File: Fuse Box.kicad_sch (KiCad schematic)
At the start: 12 parts

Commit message: HUGE TOP LEVEL
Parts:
- F?: value (none) -> Fuse 3
- F?: value (none) -> Fuse 1
- F?: value (none) -> Fuse 4
- F?: value (none) -> Fuse 2
- K? (x4): value (none) -> Relay
- U?: value (none) -> DT_12_Pin
- U? (x2): value (none) -> Bridge
- U?: value (none) -> DTM04-12pb
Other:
- note added: "CANH and CANL Not Used on Fusebox, Was 4 PDM"
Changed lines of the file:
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@@
     (stroke (width 0) (type default) (color 0 0 0 0))
   )
+  (text "CANH and CANL Not Used on Fusebox, Was 4 PDM" (at 113.792 53.848 0)
+    (effects (font (size 1.27 1.27)) (justify left bottom))
+  )
   (global_label "Fan Power" (shape input) (at 75.184 29.972 180) (fields_autoplaced)
     (effects (font (size 1.27 1.27)) (justify right))
@@
     )
   )
-  (global_label "EFI Signal" (shape input) (at 149.098 33.782 0) (fields_autoplaced)
-    (effects (font (size 1.27 1.27)) (justify left))
-    (property "Intersheet References" "${INTERSHEET_REFS}" (id 0) (at 161.2478 33.7026 0)
+  (global_label "EFI Relay Signal" (shape input) (at 149.098 33.782 0) (fields_autoplaced)
+    (effects (font (size 1.27 1.27)) (justify left))
+    (property "Intersheet References" "${INTERSHEET_REFS}" (id 0) (at 167.3559 33.7026 0)
       (effects (font (size 1.27 1.27)) (justify left) hide)
     )
@@
     (in_bom yes) (on_board yes) (fields_autoplaced)
     (property "Reference" "K?" (id 0) (at 139.8905 60.452 0))
-    (property "Value" "" (id 1) (at 139.8905 62.992 0))
+    (property "Value" "Relay" (id 1) (at 139.8905 62.992 0))
     (property "Footprint" "" (id 2) (at 173.609 76.962 0)
       (effects (font (size 1.27 1.27)) hide)
@@
     (in_bom yes) (on_board yes) (fields_autoplaced)
     (property "Reference" "F?" (id 0) (at 82.296 134.112 90))
-    (property "Value" "" (id 1) (at 82.296 136.652 90))
+    (property "Value" "Fuse 3" (id 1) (at 82.296 136.652 90))
     (property "Footprint" "" (id 2) (at 82.296 138.684 90)
       (effects (font (size 1.27 1.27)) hide)
@@
     (in_bom yes) (on_board yes) (fields_autoplaced)
     (property "Reference" "F?" (id 0) (at 82.55 57.912 90))
-    (property "Value" "" (id 1) (at 82.55 60.452 90))
+    (property "Value" "Fuse 1" (id 1) (at 82.55 60.452 90))
     (property "Footprint" "" (id 2) (at 82.55 62.484 90)
       (effects (font (size 1.27 1.27)) hide)
@@
     (in_bom yes) (on_board yes) (fields_autoplaced)
     (property "Reference" "U?" (id 0) (at 84.1121 22.352 0))
-    (property "Value" "" (id 1) (at 84.1121 24.892 0))
+    (property "Value" "DT_12_Pin" (id 1) (at 84.1121 24.892 0))
     (property "Footprint" "" (id 2) (at 83.82 50.292 0)
       (effects (font (size 1.27 1.27)) hide)
@@
     (in_bom yes) (on_board yes) (fields_autoplaced)
     (property "Reference" "K?" (id 0) (at 140.462 120.0023 0))
-    (property "Value" "" (id 1) (at 140.462 122.5423 0))
+    (property "Value" "Relay" (id 1) (at 140.462 122.5423 0))
     (property "Footprint" "" (id 2) (at 174.1805 136.5123 0)
       (effects (font (size 1.27 1.27)) hide)
@@
       (effects (font (size 1.27 1.27)) (justify right))
     )
-    (property "Value" "" (id 1) (at 115.062 110.7439 90)
+    (property "Value" "Bridge" (id 1) (at 115.062 110.7439 90)
       (effects (font (size 1.27 1.27)) (justify right))
     )
@@
     (in_bom yes) (on_board yes) (fields_autoplaced)
     (property "Reference" "F?" (id 0) (at 82.55 162.56 90))
-    (property "Value" "" (id 1) (at 82.55 165.1 90))
+    (property "Value" "Fuse 4" (id 1) (at 82.55 165.1 90))
     (property "Footprint" "" (id 2) (at 82.55 167.132 90)
       (effects (font (size 1.27 1.27)) hide)
@@
     (in_bom yes) (on_board yes) (fields_autoplaced)
     (property "Reference" "U?" (id 0) (at 139.9921 22.098 0))
-    (property "Value" "" (id 1) (at 139.9921 24.638 0))
+    (property "Value" "DTM04-12pb" (id 1) (at 139.9921 24.638 0))
     (property "Footprint" "" (id 2) (at 139.7 50.292 0)
       (effects (font (size 1.27 1.27)) hide)
@@
     (in_bom yes) (on_board yes) (fields_autoplaced)
     (property "Reference" "K?" (id 0) (at 140.97 148.7043 0))
-    (property "Value" "" (id 1) (at 140.97 151.2443 0))
+    (property "Value" "Relay" (id 1) (at 140.97 151.2443 0))
     (property "Footprint" "" (id 2) (at 174.6885 165.2143 0)
       (effects (font (size 1.27 1.27)) hide)
@@
       (effects (font (size 1.27 1.27)) (justify right))
     )
-    (property "Value" "" (id 1) (at 115.062 141.9859 90)
+    (property "Value" "Bridge" (id 1) (at 115.062 141.9859 90)
       (effects (font (size 1.27 1.27)) (justify right))
     )
@@
     (in_bom yes) (on_board yes) (fields_autoplaced)
     (property "Reference" "K?" (id 0) (at 140.1445 89.408 0))
-    (property "Value" "" (id 1) (at 140.1445 91.948 0))
+    (property "Value" "Relay" (id 1) (at 140.1445 91.948 0))
     (property "Footprint" "" (id 2) (at 173.863 105.918 0)
       (effects (font (size 1.27 1.27)) hide)
@@
     (in_bom yes) (on_board yes) (fields_autoplaced)
     (property "Reference" "F?" (id 0) (at 82.55 74.676 90))
-    (property "Value" "" (id 1) (at 82.55 77.216 90))
+    (property "Value" "Fuse 2" (id 1) (at 82.55 77.216 90))
     (property "Footprint" "" (id 2) (at 82.55 79.248 90)
       (effects (font (size 1.27 1.27)) hide)

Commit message: Filled in Many Sheets
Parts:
- U?: value DT_12_Pin -> DT_12P_BLACK_FEMALE
- U?: value DTM04-12pb -> DTM_12P_BLACK_MALE
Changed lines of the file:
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@@
   (symbol (lib_name "DTM_12_Pin_2") (lib_id "SCR23 Library:DTM_12_Pin") (at 83.82 40.132 0) (unit 1)
     (in_bom yes) (on_board yes) (fields_autoplaced)
-    (property "Reference" "U?" (id 0) (at 84.1121 22.352 0))
-    (property "Value" "DT_12_Pin" (id 1) (at 84.1121 24.892 0))
+    (property "Reference" "U?" (id 0) (at 84.1121 21.59 0)
+      (effects (font (size 1.27 1.27)) hide)
+    )
+    (property "Value" "DT_12P_BLACK_FEMALE" (id 1) (at 84.1121 24.13 0))
     (property "Footprint" "" (id 2) (at 83.82 50.292 0)
       (effects (font (size 1.27 1.27)) hide)
@@
   (symbol (lib_id "SCR23 Library:DTM04-12pb") (at 139.7 40.132 0) (unit 1)
     (in_bom yes) (on_board yes) (fields_autoplaced)
-    (property "Reference" "U?" (id 0) (at 139.9921 22.098 0))
-    (property "Value" "DTM04-12pb" (id 1) (at 139.9921 24.638 0))
+    (property "Reference" "U?" (id 0) (at 139.9921 21.59 0)
+      (effects (font (size 1.27 1.27)) hide)
+    )
+    (property "Value" "DTM_12P_BLACK_MALE" (id 1) (at 139.9921 24.13 0))
     (property "Footprint" "" (id 2) (at 139.7 50.292 0)
       (effects (font (size 1.27 1.27)) hide)

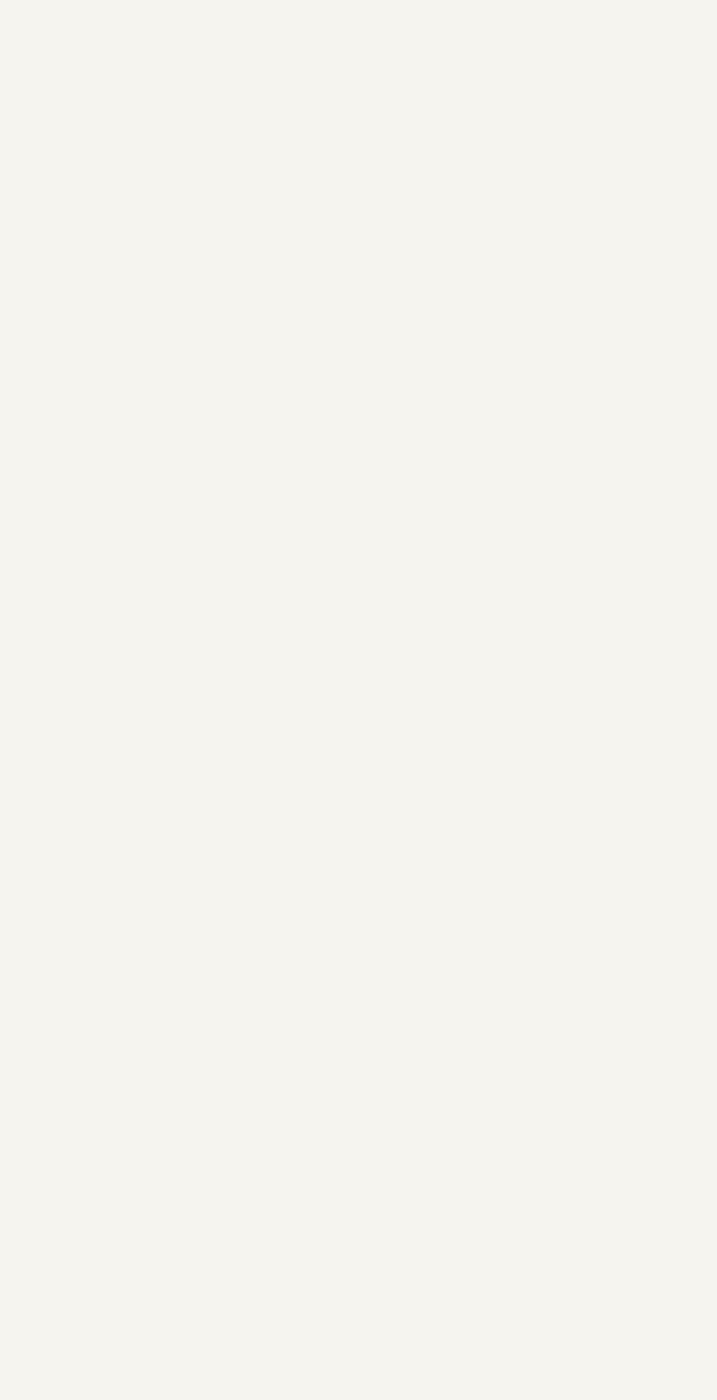
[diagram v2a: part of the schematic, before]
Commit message: Updated Connectors
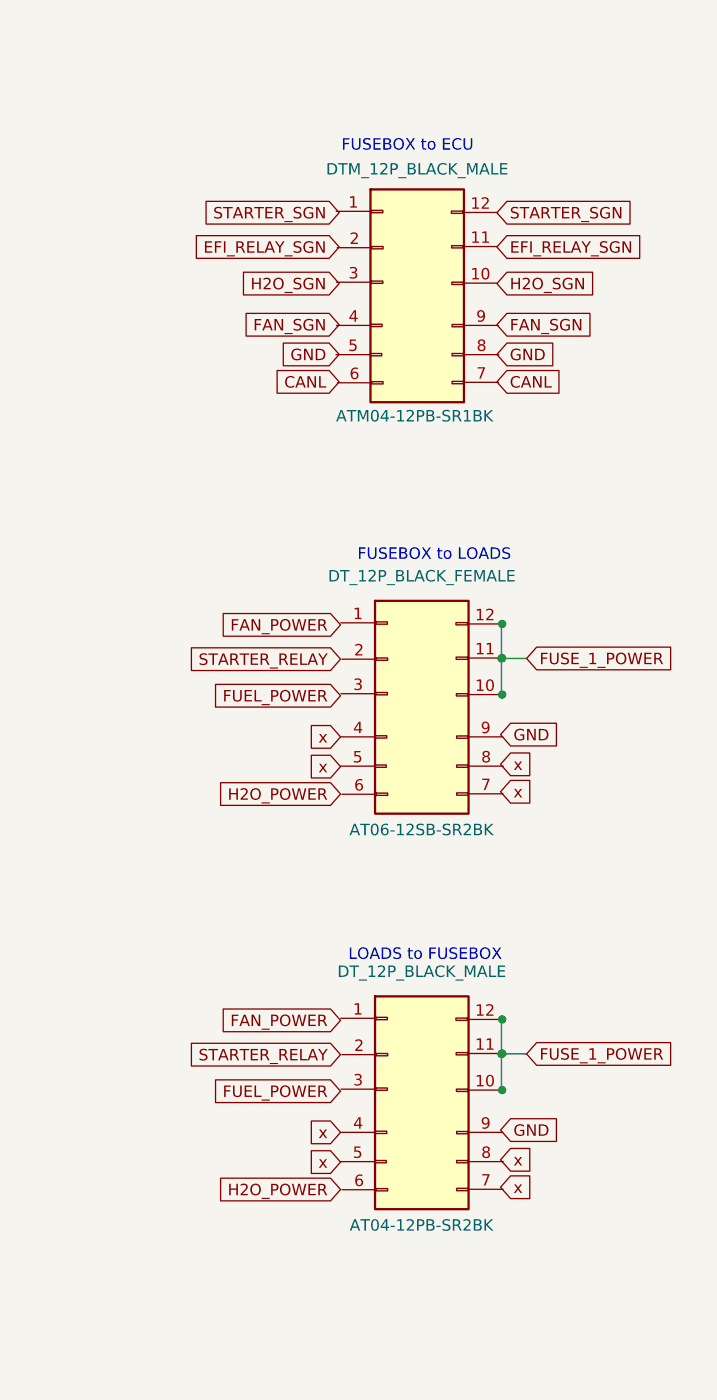
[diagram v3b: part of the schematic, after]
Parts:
- added U?: DT_12P_BLACK_FEMALE, symbol SCR23 Library:DTM04-12pb
- added U?: DTM_12P_BLACK_MALE, symbol SCR23 Library:DTM04-12pb
- added U?: DT_12P_BLACK_MALE, symbol SCR23 Library:DTM04-12pb
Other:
- note added: "FUSEBOX to ECU"
- note added: "FUSEBOX to LOADS"
- note added: "LOADS to FUSEBOX"

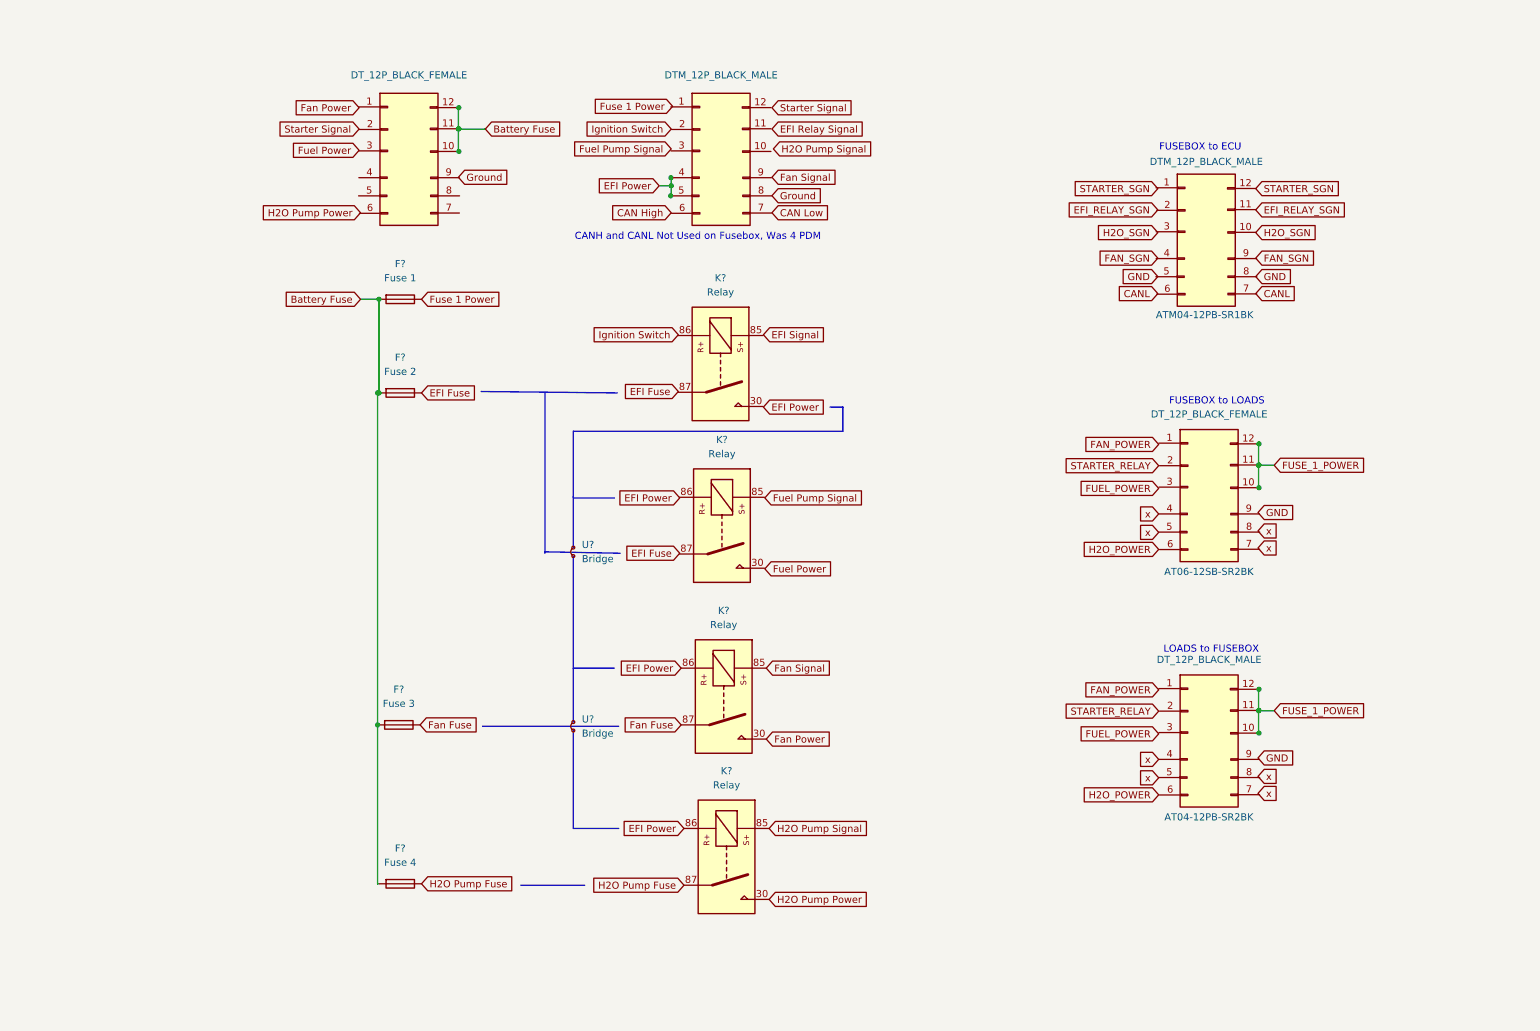
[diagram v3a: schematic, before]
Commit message: Updated Connectors
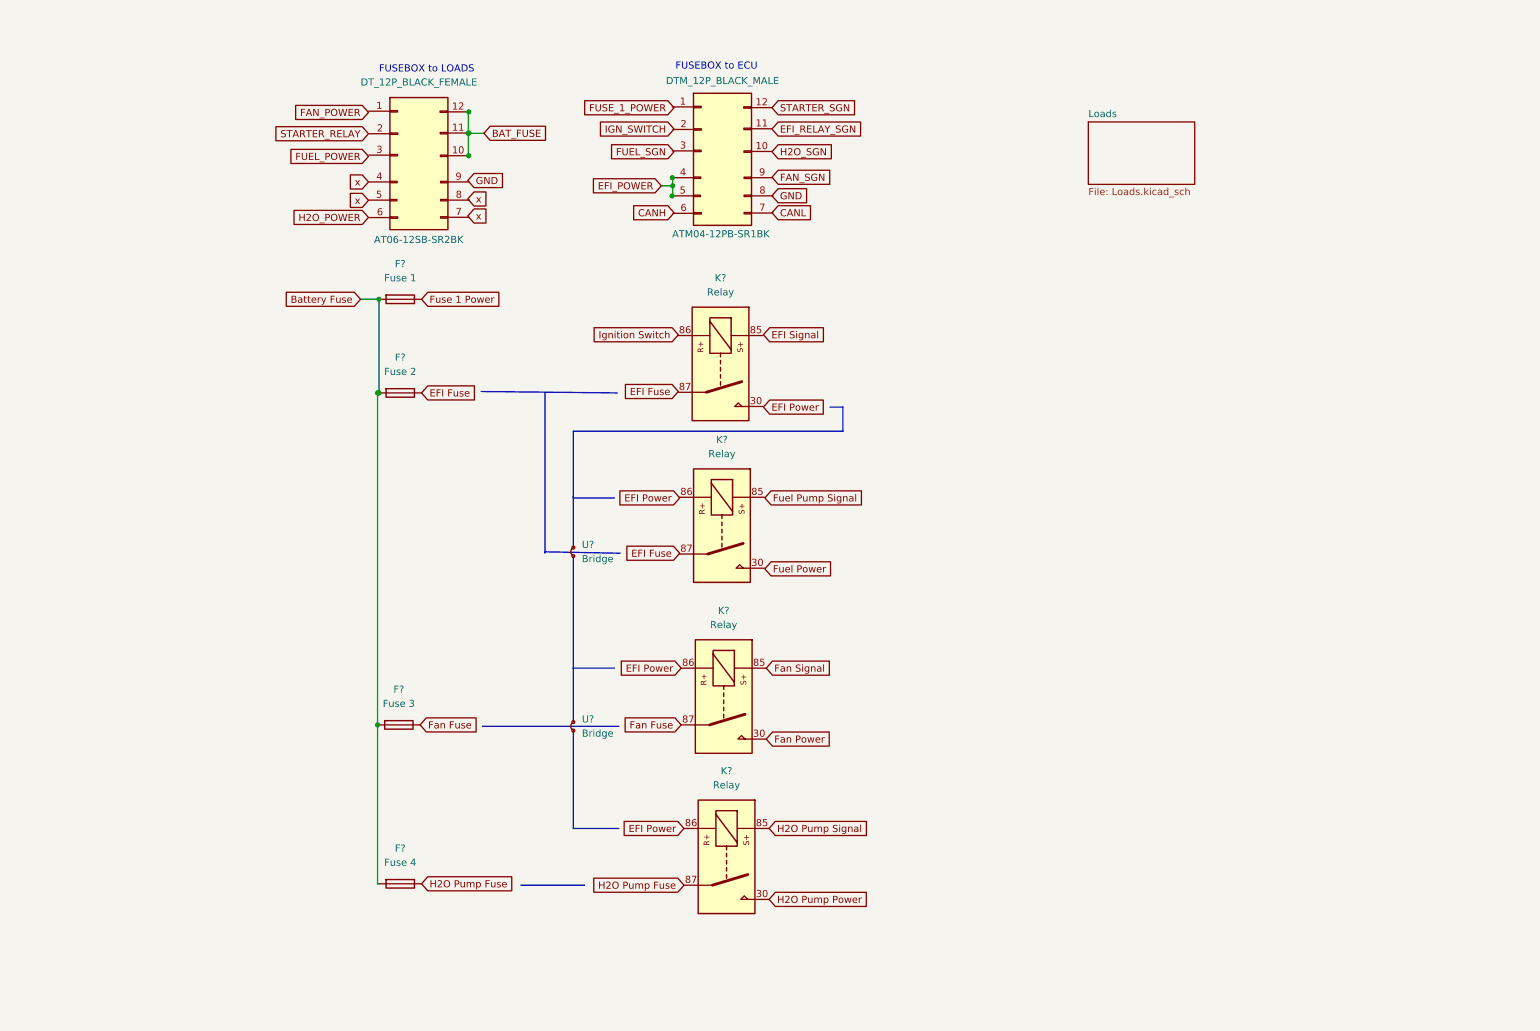
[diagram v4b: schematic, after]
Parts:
- removed U?: DT_12P_BLACK_FEMALE, symbol SCR23 Library:DTM_12_Pin
- removed U?: DTM_12P_BLACK_MALE, symbol SCR23 Library:DTM04-12pb
- removed U?: DT_12P_BLACK_MALE, symbol SCR23 Library:DTM04-12pb
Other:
- added sheet Loads (Loads.kicad_sch)
- note removed: "CANH and CANL Not Used on Fusebox, Was 4 PDM"
- note removed: "LOADS to FUSEBOX"

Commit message: readd all connectors
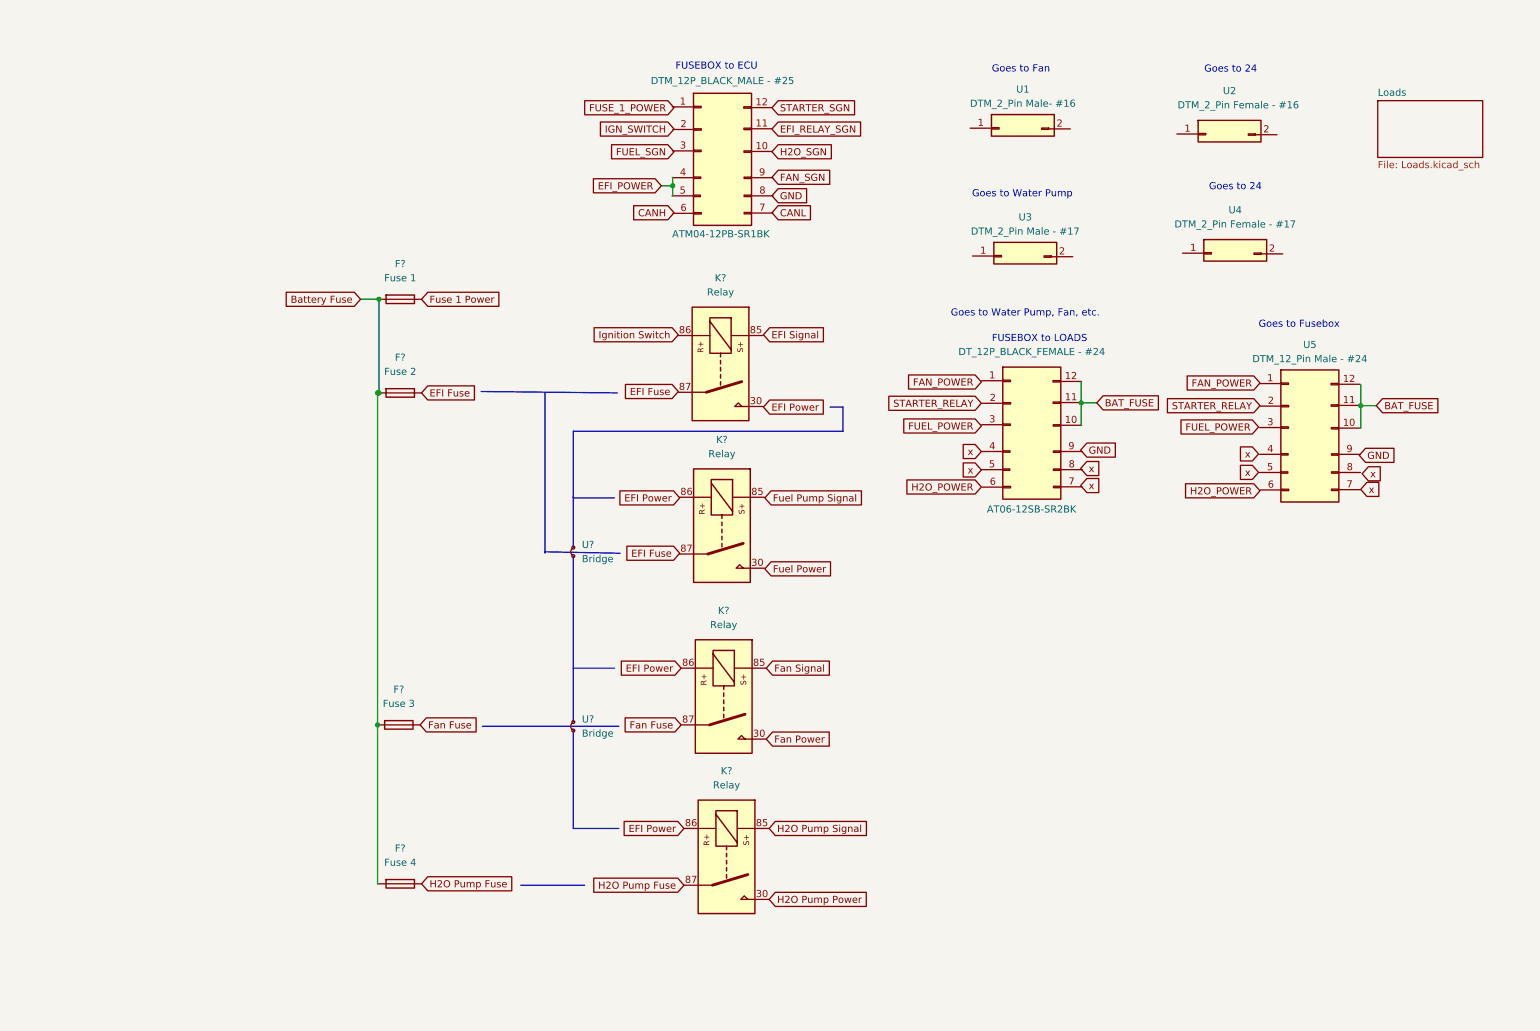
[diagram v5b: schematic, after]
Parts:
- added U1: DTM_2_Pin Male- #16, symbol SCR23 Library:DTM_2_Pin
- added U2: DTM_2_Pin Female - #16, symbol SCR23 Library:DTM_2_Pin
- added U3: DTM_2_Pin Male - #17, symbol SCR23 Library:DTM_2_Pin
- added U4: DTM_2_Pin Female - #17, symbol SCR23 Library:DTM_2_Pin
- added U5: DTM_12_Pin Male - #24, symbol SCR23 Library:DTM_12_Pin
- U?: value DT_12P_BLACK_FEMALE -> DT_12P_BLACK_FEMALE - #24
- U?: value DTM_12P_BLACK_MALE -> DTM_12P_BLACK_MALE - #25
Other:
- note added: "Goes to 24"
- note added: "Goes to Fan"
- note added: "Goes to Fusebox"
- note added: "Goes to Water Pump"
- note added: "Goes to Water Pump, Fan, etc."
